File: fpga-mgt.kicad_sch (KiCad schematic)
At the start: 50 parts, among them U34 XCAU25P-2FFVB676I, U39 SI5319C-C-GM-ND, Y4 Resonator_114.285MHZ_ABM8

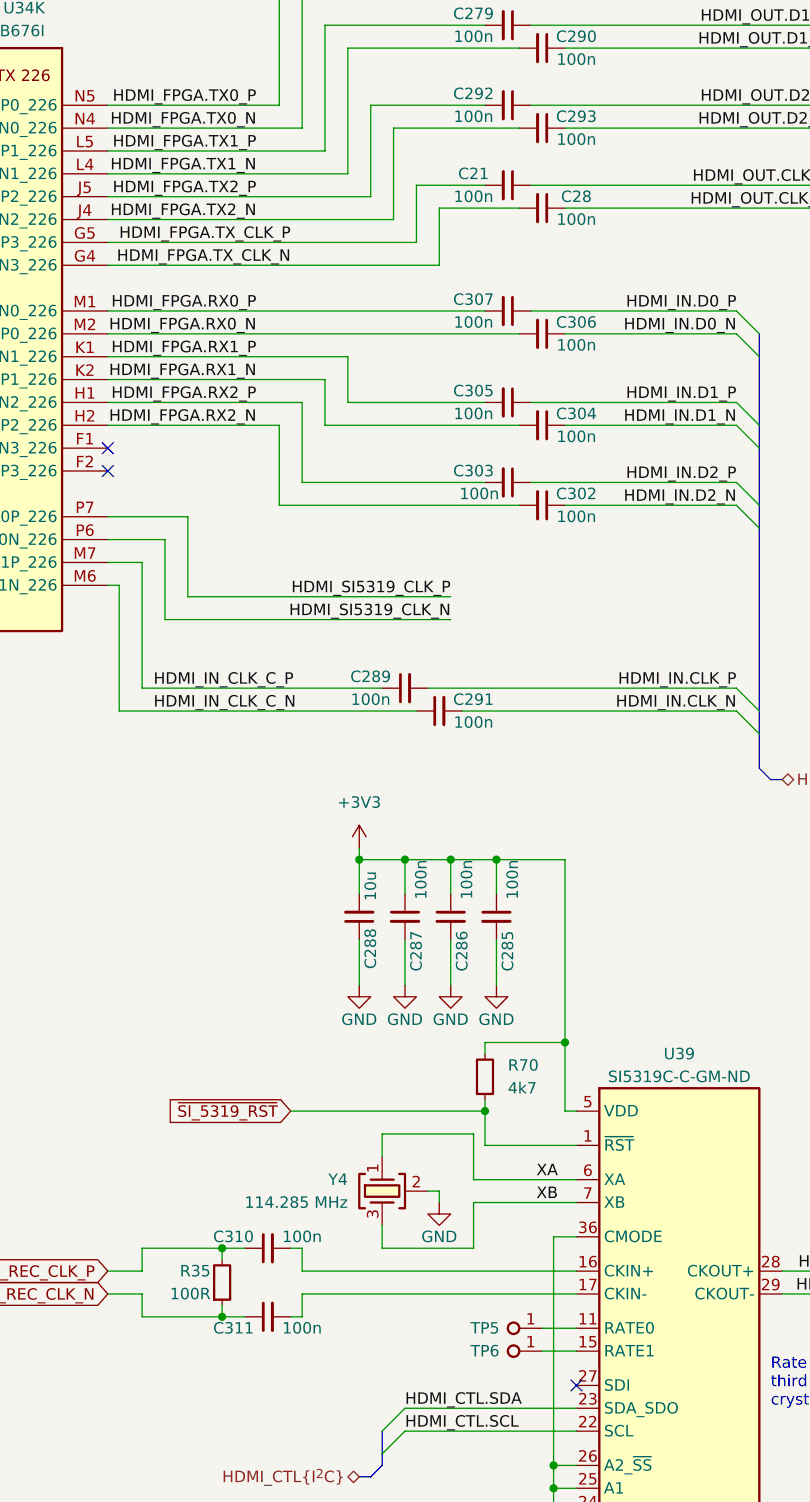
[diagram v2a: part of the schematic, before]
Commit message: [#66727] Fix schematic errors
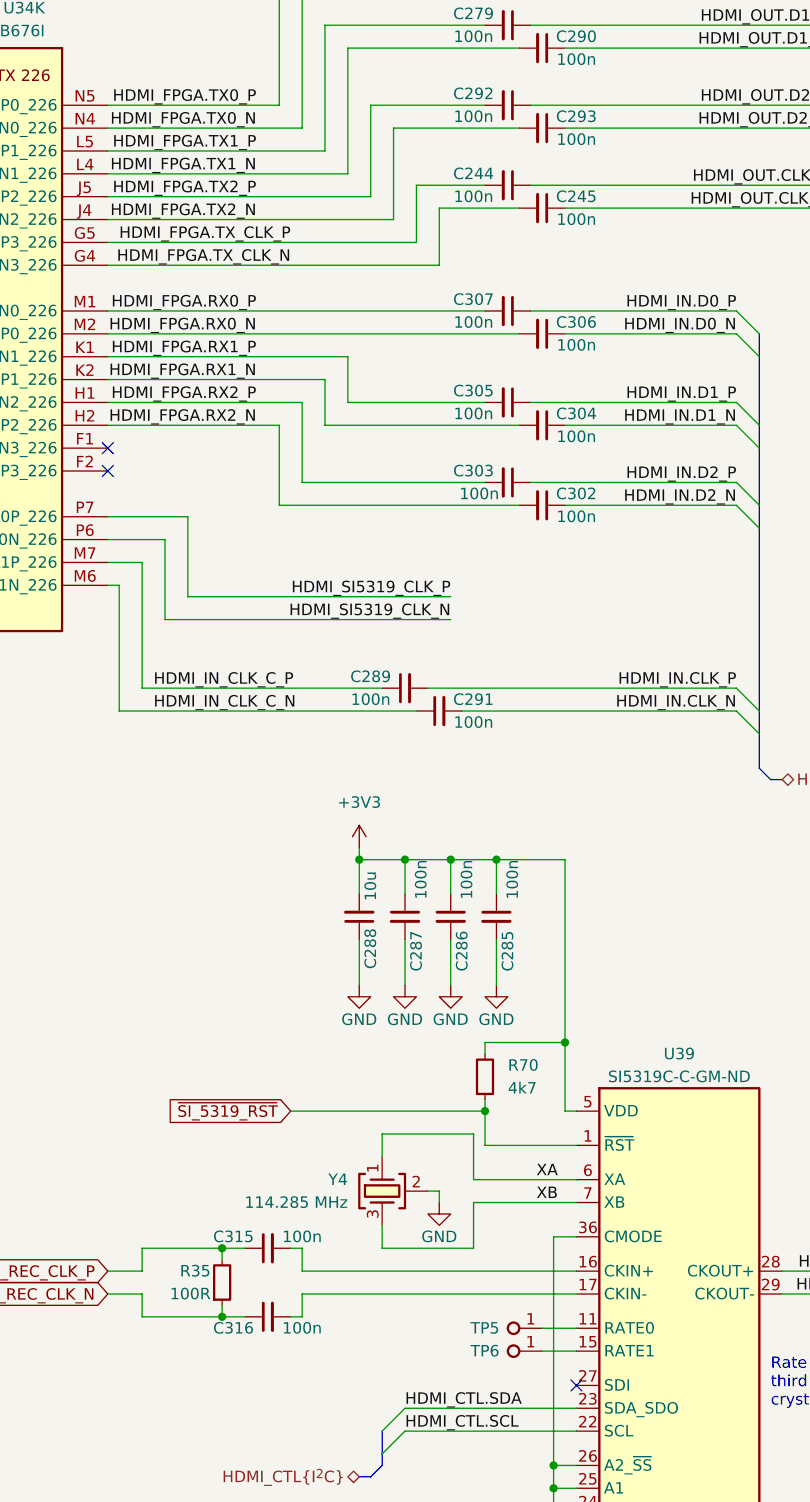
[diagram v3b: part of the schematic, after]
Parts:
- renumbered C21 to C244, C28 to C245, C310 to C315, C311 to C316
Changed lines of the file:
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@@
   (symbol (lib_id "antmicroCapacitors0402:C_100n_0402") (at 274.32 196.85 0) (unit 1)
     (in_bom yes) (on_board yes) (dnp no)
-    (property "Reference" "C310" (at 273.05 195.58 0)
+    (property "Reference" "C315" (at 273.05 195.58 0)
       (effects (font (size 1.27 1.27) (thickness 0.15)))
     )
@@
       (project "data-center-rdimm-ddr5-tester"
         (path "/1faa6543-e26a-4449-8bac-ee14b9f19e5f/e98c799f-d02e-47b6-ad5c-871bd722b830"
-          (reference "C310") (unit 1)
+          (reference "C315") (unit 1)
         )
       )
@@
   (symbol (lib_id "antmicroCapacitors0402:C_100n_0402") (at 306.07 78.74 0) (mirror y) (unit 1)
     (in_bom yes) (on_board yes) (dnp no)
-    (property "Reference" "C21" (at 299.72 77.47 0)
+    (property "Reference" "C244" (at 299.72 77.47 0)
       (effects (font (size 1.27 1.27)))
     )
@@
       (project "data-center-rdimm-ddr5-tester"
         (path "/1faa6543-e26a-4449-8bac-ee14b9f19e5f/e98c799f-d02e-47b6-ad5c-871bd722b830"
-          (reference "C21") (unit 1)
+          (reference "C244") (unit 1)
         )
       )
@@
   (symbol (lib_id "antmicroCapacitors0402:C_100n_0402") (at 309.88 81.28 0) (mirror y) (unit 1)
     (in_bom yes) (on_board yes) (dnp no)
-    (property "Reference" "C28" (at 311.15 80.01 0)
+    (property "Reference" "C245" (at 311.15 80.01 0)
       (effects (font (size 1.27 1.27)))
     )
@@
       (project "data-center-rdimm-ddr5-tester"
         (path "/1faa6543-e26a-4449-8bac-ee14b9f19e5f/e98c799f-d02e-47b6-ad5c-871bd722b830"
-          (reference "C28") (unit 1)
+          (reference "C245") (unit 1)
         )
       )
@@
   (symbol (lib_name "GND_1") (lib_id "antmicropower:GND") (at 308.61 236.22 0) (unit 1)
     (in_bom yes) (on_board yes) (dnp no)
-    (property "Reference" "#PWR0463" (at 317.5 238.76 0)
+    (property "Reference" "#PWR0425" (at 317.5 238.76 0)
       (effects (font (size 1.27 1.27) (thickness 0.15)) (justify left bottom) hide)
     )
@@
       (project "data-center-rdimm-ddr5-tester"
         (path "/1faa6543-e26a-4449-8bac-ee14b9f19e5f/e98c799f-d02e-47b6-ad5c-871bd722b830"
-          (reference "#PWR0463") (unit 1)
+          (reference "#PWR0425") (unit 1)
         )
       )
@@
     (pin "27")
     (pin "1")
-    (pin "51")
+    (pin "14")
     (pin "5")
     (pin "28")
@@
     (pin "23")
     (pin "2")
-    (pin "55")
+    (pin "35")
     (pin "20")
     (pin "26")
     (pin "36")
-    (pin "57")
+    (pin "12")
     (pin "6")
     (pin "9")
@@
     (pin "22")
     (pin "11")
-    (pin "52")
-    (pin "53")
-    (pin "56")
-    (pin "54")
+    (pin "33")
+    (pin "13")
+    (pin "30")
+    (pin "34")
     (pin "16")
     (pin "18")
@@
   (symbol (lib_name "GND_1") (lib_id "antmicropower:GND") (at 304.8 236.22 0) (unit 1)
     (in_bom yes) (on_board yes) (dnp no)
-    (property "Reference" "#PWR0462" (at 313.69 238.76 0)
+    (property "Reference" "#PWR0373" (at 313.69 238.76 0)
       (effects (font (size 1.27 1.27) (thickness 0.15)) (justify left bottom) hide)
     )
@@
       (project "data-center-rdimm-ddr5-tester"
         (path "/1faa6543-e26a-4449-8bac-ee14b9f19e5f/e98c799f-d02e-47b6-ad5c-871bd722b830"
-          (reference "#PWR0462") (unit 1)
+          (reference "#PWR0373") (unit 1)
         )
       )
@@
   (symbol (lib_id "antmicroCapacitors0402:C_100n_0402") (at 274.32 204.47 0) (mirror x) (unit 1)
     (in_bom yes) (on_board yes) (dnp no)
-    (property "Reference" "C311" (at 273.05 205.74 0)
+    (property "Reference" "C316" (at 273.05 205.74 0)
       (effects (font (size 1.27 1.27) (thickness 0.15)))
     )
@@
       (project "data-center-rdimm-ddr5-tester"
         (path "/1faa6543-e26a-4449-8bac-ee14b9f19e5f/e98c799f-d02e-47b6-ad5c-871bd722b830"
-          (reference "C311") (unit 1)
+          (reference "C316") (unit 1)
         )
       )

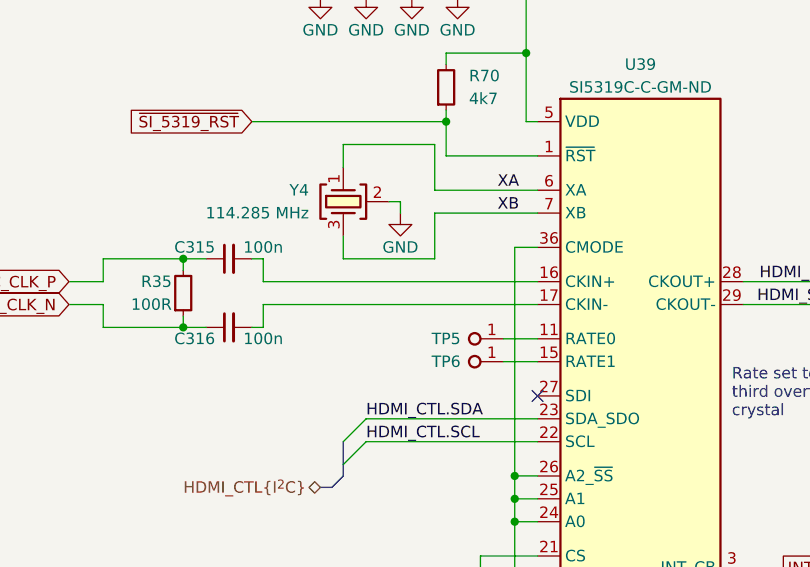
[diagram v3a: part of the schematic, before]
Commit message: [#65754] Route HDMI
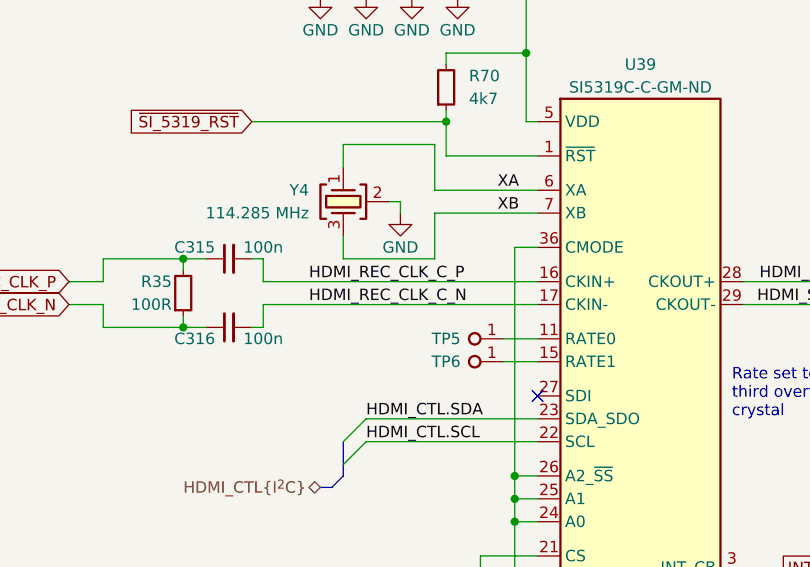
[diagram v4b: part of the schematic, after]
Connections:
- net HDMI_REC_CLK_C_P: now reaches C315.2, U39.16 (CKIN+)
- net HDMI_REC_CLK_C_N: now reaches C316.2, U39.17 (CKIN-)
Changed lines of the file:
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@@
     (effects (font (size 1.27 1.27)) (justify right bottom))
+  )
+  (label "HDMI_REC_CLK_C_N" (at 285.75 201.93 0) (fields_autoplaced)
+    (effects (font (size 1.27 1.27)) (justify left bottom))
   )
   (label "HDMI_OUT.CLK_P" (at 339.09 78.74 180) (fields_autoplaced)
@@
     (effects (font (size 1.27 1.27)) (justify right bottom))
   )
+  (label "HDMI_REC_CLK_C_P" (at 285.75 199.39 0) (fields_autoplaced)
+    (effects (font (size 1.27 1.27)) (justify left bottom))
+  )
   (label "GTY_224_RX0_P" (at 86.36 96.52 180) (fields_autoplaced)

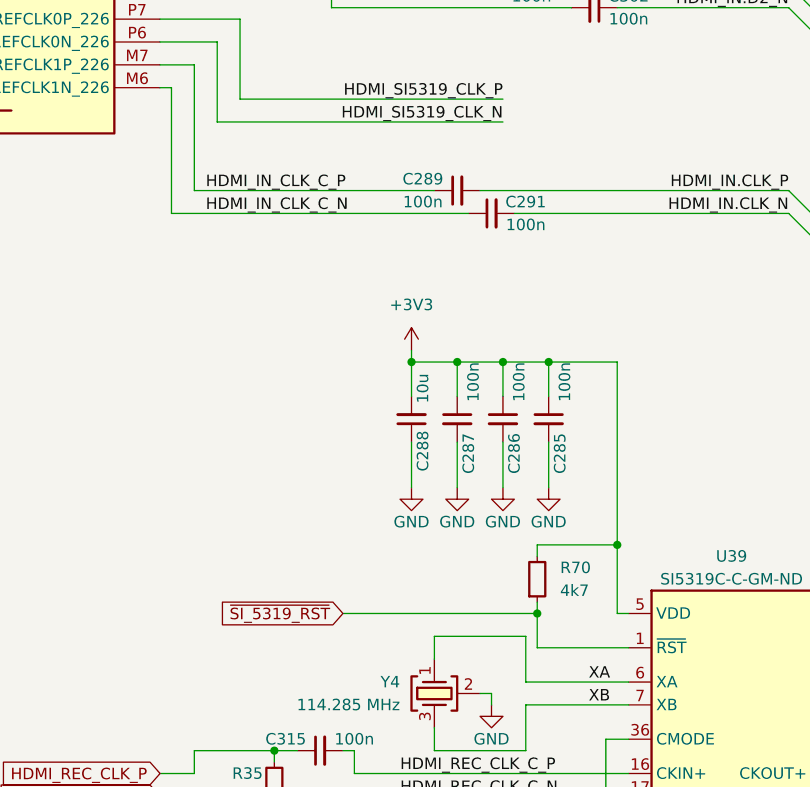
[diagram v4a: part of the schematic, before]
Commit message: [#67402] Connect low speed signals and interfaces to the HD banks. Optimize connection in bank 86
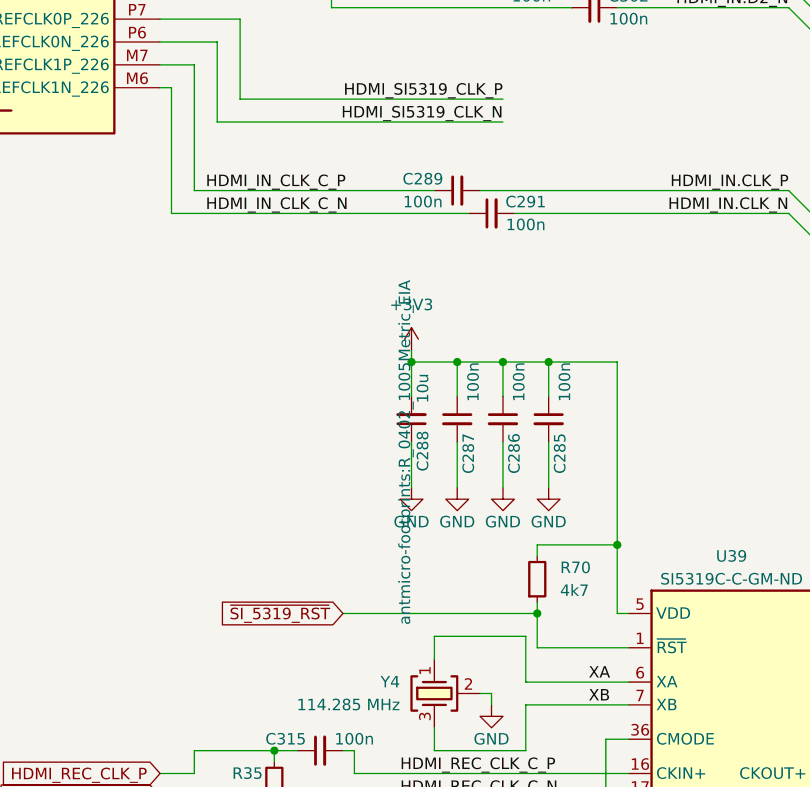
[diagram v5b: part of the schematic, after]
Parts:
- R35: footprint antmicro-footprints:R_0402_1005Metric -> antmicro-footprints:R_0402_1005Metric_EIA
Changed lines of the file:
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@@
       (effects (font (size 1.27 1.27) (thickness 0.15)) (justify left bottom) hide)
     )
-    (property "Footprint" "antmicro-footprints:R_0402_1005Metric" (at 287.02 182.88 0)
-      (effects (font (size 1.27 1.27) (thickness 0.15)) (justify left bottom) hide)
+    (property "Footprint" "antmicro-footprints:R_0402_1005Metric_EIA" (at 287.02 182.88 0)
+      (effects (font (size 1.27 1.27) (thickness 0.15)) (justify left bottom))
     )
     (property "Datasheet" "https://www.bourns.com/docs/product-datasheets/cr.pdf" (at 289.56 182.88 0)

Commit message: [#67725] Update fpga-mgt sheet - change HDMI connection
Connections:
- net HDMI_FPGA.RX0_N: now also U34.M1 (MGTYRXN0_226); no longer U34.M2 (MGTYRXP0_226)
- net HDMI_FPGA.RX0_P: now also U34.M2 (MGTYRXP0_226); no longer U34.M1 (MGTYRXN0_226)
- net HDMI_FPGA.RX1_N: now also U34.K1 (MGTYRXN1_226); no longer U34.K2 (MGTYRXP1_226)
- net HDMI_FPGA.RX1_P: now also U34.K2 (MGTYRXP1_226); no longer U34.K1 (MGTYRXN1_226)
- net HDMI_FPGA.RX2_N: now also U34.H1 (MGTYRXN2_226); no longer U34.H2 (MGTYRXP2_226)
- net HDMI_FPGA.RX2_P: now also U34.H2 (MGTYRXP2_226); no longer U34.H1 (MGTYRXN2_226)
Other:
- note added: "Clock multipler"
- note added: "I2C: 0x68"
- moved on the sheet: C222, C226, C227, C228, C229, C230, C231, C232, C233, C244, C245, C250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
